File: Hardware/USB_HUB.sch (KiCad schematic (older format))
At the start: 23 parts, among them U1 USB2514B_Bi, U2 MIC2026-1BM, U3 MIC2026-1BM, Y1 24 MHz

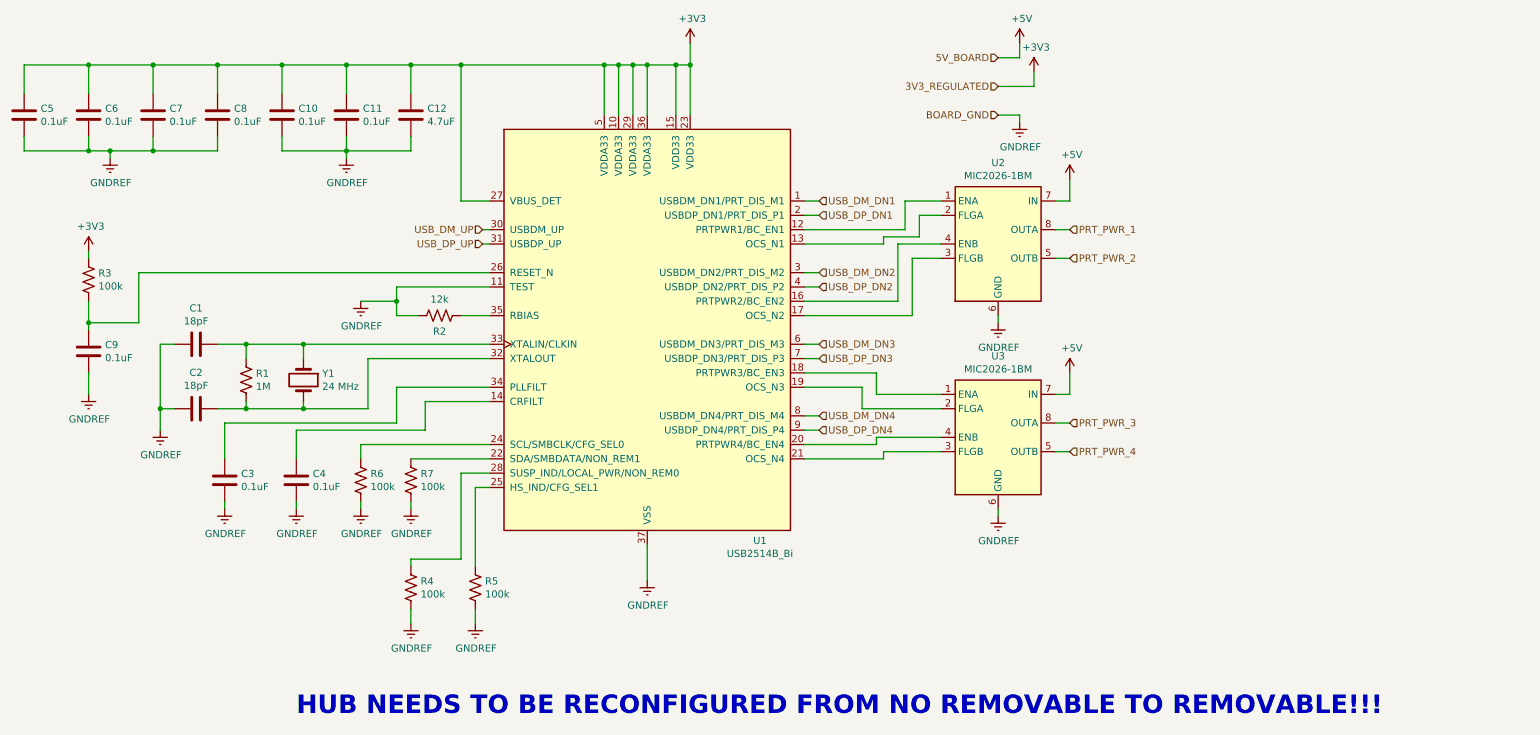
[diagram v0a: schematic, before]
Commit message: Added footprints to schematic symbols
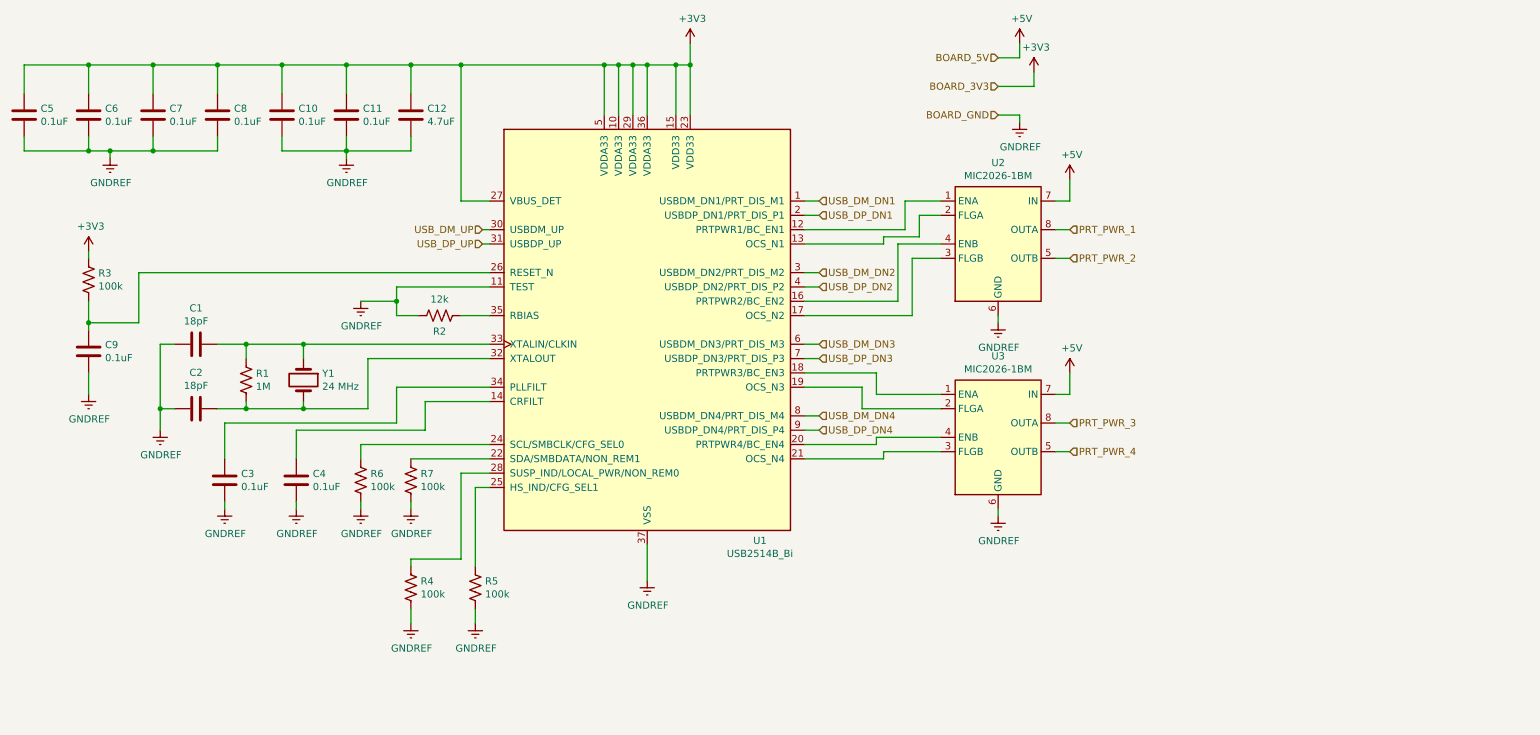
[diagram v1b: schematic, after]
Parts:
- C1, C2, C7: footprint (none) -> Capacitor_SMD:C_0603_1608Metric
- R1, R2, R3, R4, R5, R6, R7: footprint (none) -> Resistor_SMD:R_1206_3216Metric
- U3: footprint (none) -> Package_SO:SOIC-8_3.9x4.9mm_P1.27mm
- Y1: footprint (none) -> Crystal:Crystal_SMD_3225-4Pin_3.2x2.5mm
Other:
- note removed: "HUB NEEDS TO BE RECONFIGURED FROM NO REMOVABLE TO REMOVABLE!!!"
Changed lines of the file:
@@
 F 0 "Y1" V 2704 3331 50  0000 L CNN
 F 1 "24 MHz " V 2795 3331 50  0000 L CNN
-F 2 "" H 2750 3200 50  0001 C CNN
+F 2 "Crystal:Crystal_SMD_3225-4Pin_3.2x2.5mm" H 2750 3200 50  0001 C CNN
 F 3 "~" H 2750 3200 50  0001 C CNN
 	1    2750 3200
@@
 F 0 "C1" V 1748 2950 50  0000 C CNN
 F 1 "18pF" V 1839 2950 50  0000 C CNN
-F 2 "" H 2038 2800 50  0001 C CNN
+F 2 "Capacitor_SMD:C_0603_1608Metric" H 2038 2800 50  0001 C CNN
 F 3 "~" H 2000 2950 50  0001 C CNN
 	1    2000 2950
@@
 F 0 "C2" V 1748 3400 50  0000 C CNN
 F 1 "18pF" V 1839 3400 50  0000 C CNN
-F 2 "" H 2038 3250 50  0001 C CNN
+F 2 "Capacitor_SMD:C_0603_1608Metric" H 2038 3250 50  0001 C CNN
 F 3 "~" H 2000 3400 50  0001 C CNN
 	1    2000 3400
@@
 F 0 "R1" H 2418 3246 50  0000 L CNN
 F 1 "1M" H 2418 3155 50  0000 L CNN
-F 2 "" V 2390 3190 50  0001 C CNN
+F 2 "Resistor_SMD:R_1206_3216Metric" V 2390 3190 50  0001 C CNN
 F 3 "~" H 2350 3200 50  0001 C CNN
 	1    2350 3200
@@
 F 0 "C7" H 1815 1396 50  0000 L CNN
 F 1 "0.1uF" H 1815 1305 50  0000 L CNN
-F 2 "" H 1738 1200 50  0001 C CNN
+F 2 "Capacitor_SMD:C_0603_1608Metric" H 1738 1200 50  0001 C CNN
 F 3 "~" H 1700 1350 50  0001 C CNN
 	1    1700 1350
@@
 F 0 "U3" H 7600 4167 50  0000 C CNN
 F 1 "MIC2026-1BM" H 7600 4076 50  0000 C CNN
-F 2 "" H 7600 3600 50  0001 C CNN
+F 2 "Package_SO:SOIC-8_3.9x4.9mm_P1.27mm" H 7600 3600 50  0001 C CNN
 F 3 "http://ww1.microchip.com/downloads/en/DeviceDoc/mic2026.pdf" H 7600 3600 50  0001 C CNN
 	1    7600 3600
@@
 	8100 3700 8000 3700
 Text HLabel 7600 950  0    50   Input ~ 0
-5V_BOARD
+BOARD_5V
 Text HLabel 7600 1150 0    50   Input ~ 0
-3V3_REGULATED
+BOARD_3V3
 $Comp
 L power:+5V #PWR0115
@@
 F 0 "R6" H 3218 3946 50  0000 L CNN
 F 1 "100k" H 3218 3855 50  0000 L CNN
-F 2 "" V 3190 3890 50  0001 C CNN
+F 2 "Resistor_SMD:R_1206_3216Metric" V 3190 3890 50  0001 C CNN
 F 3 "~" H 3150 3900 50  0001 C CNN
 	1    3150 3900
@@
 F 0 "R7" H 3568 3946 50  0000 L CNN
 F 1 "100k" H 3568 3855 50  0000 L CNN
-F 2 "" V 3540 3890 50  0001 C CNN
+F 2 "Resistor_SMD:R_1206_3216Metric" V 3540 3890 50  0001 C CNN
 F 3 "~" H 3500 3900 50  0001 C CNN
 	1    3500 3900
@@
 F 0 "R5" H 4018 4696 50  0000 L CNN
 F 1 "100k" H 4018 4605 50  0000 L CNN
-F 2 "" V 3990 4640 50  0001 C CNN
+F 2 "Resistor_SMD:R_1206_3216Metric" V 3990 4640 50  0001 C CNN
 F 3 "~" H 3950 4650 50  0001 C CNN
 	1    3950 4650
@@
 F 0 "R2" V 3810 2750 50  0000 C CNN
 F 1 "12k" V 3586 2750 50  0000 C CNN
-F 2 "" V 3740 2740 50  0001 C CNN
+F 2 "Resistor_SMD:R_1206_3216Metric" V 3740 2740 50  0001 C CNN
 F 3 "~" H 3700 2750 50  0001 C CNN
 	1    3700 2750
@@
 F 0 "R3" H 1318 2546 50  0000 L CNN
 F 1 "100k" H 1318 2455 50  0000 L CNN
-F 2 "" V 1290 2490 50  0001 C CNN
+F 2 "Resistor_SMD:R_1206_3216Metric" V 1290 2490 50  0001 C CNN
 F 3 "~" H 1250 2500 50  0001 C CNN
 	1    1250 2500
@@
 F 0 "R4" H 3568 4696 50  0000 L CNN
 F 1 "100k" H 3568 4605 50  0000 L CNN
-F 2 "" V 3540 4640 50  0001 C CNN
+F 2 "Resistor_SMD:R_1206_3216Metric" V 3540 4640 50  0001 C CNN
 F 3 "~" H 3500 4650 50  0001 C CNN
 	1    3500 4650
@@
 Wire Wire Line
 	3950 3950 3950 4500
-Text Notes 2700 5550 0    129  ~ 26
-HUB NEEDS TO BE RECONFIGURED FROM NO REMOVABLE TO REMOVABLE!!!
 Wire Wire Line
 	3500 3750 4050 3750
@@
 	3500 4450 3500 4500
 $Comp
-L power:GNDREF #PWR?
+L power:GNDREF #PWR0145
 U 1 1 5E5C69A8
 P 3500 4100
-F 0 "#PWR?" H 3500 3850 50  0001 C CNN
+F 0 "#PWR0145" H 3500 3850 50  0001 C CNN
 F 1 "GNDREF" H 3505 3927 50  0000 C CNN
 F 2 "" H 3500 4100 50  0001 C CNN
@@
 $EndComp
 $Comp
-L power:GNDREF #PWR?
+L power:GNDREF #PWR0146
 U 1 1 5E5C6D8B
 P 3500 4900
-F 0 "#PWR?" H 3500 4650 50  0001 C CNN
+F 0 "#PWR0146" H 3500 4650 50  0001 C CNN
 F 1 "GNDREF" H 3505 4727 50  0000 C CNN
 F 2 "" H 3500 4900 50  0001 C CNN
